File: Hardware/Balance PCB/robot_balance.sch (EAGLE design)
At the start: 49 parts, among them P1 10118194-0001LF, Q1 16Mhz

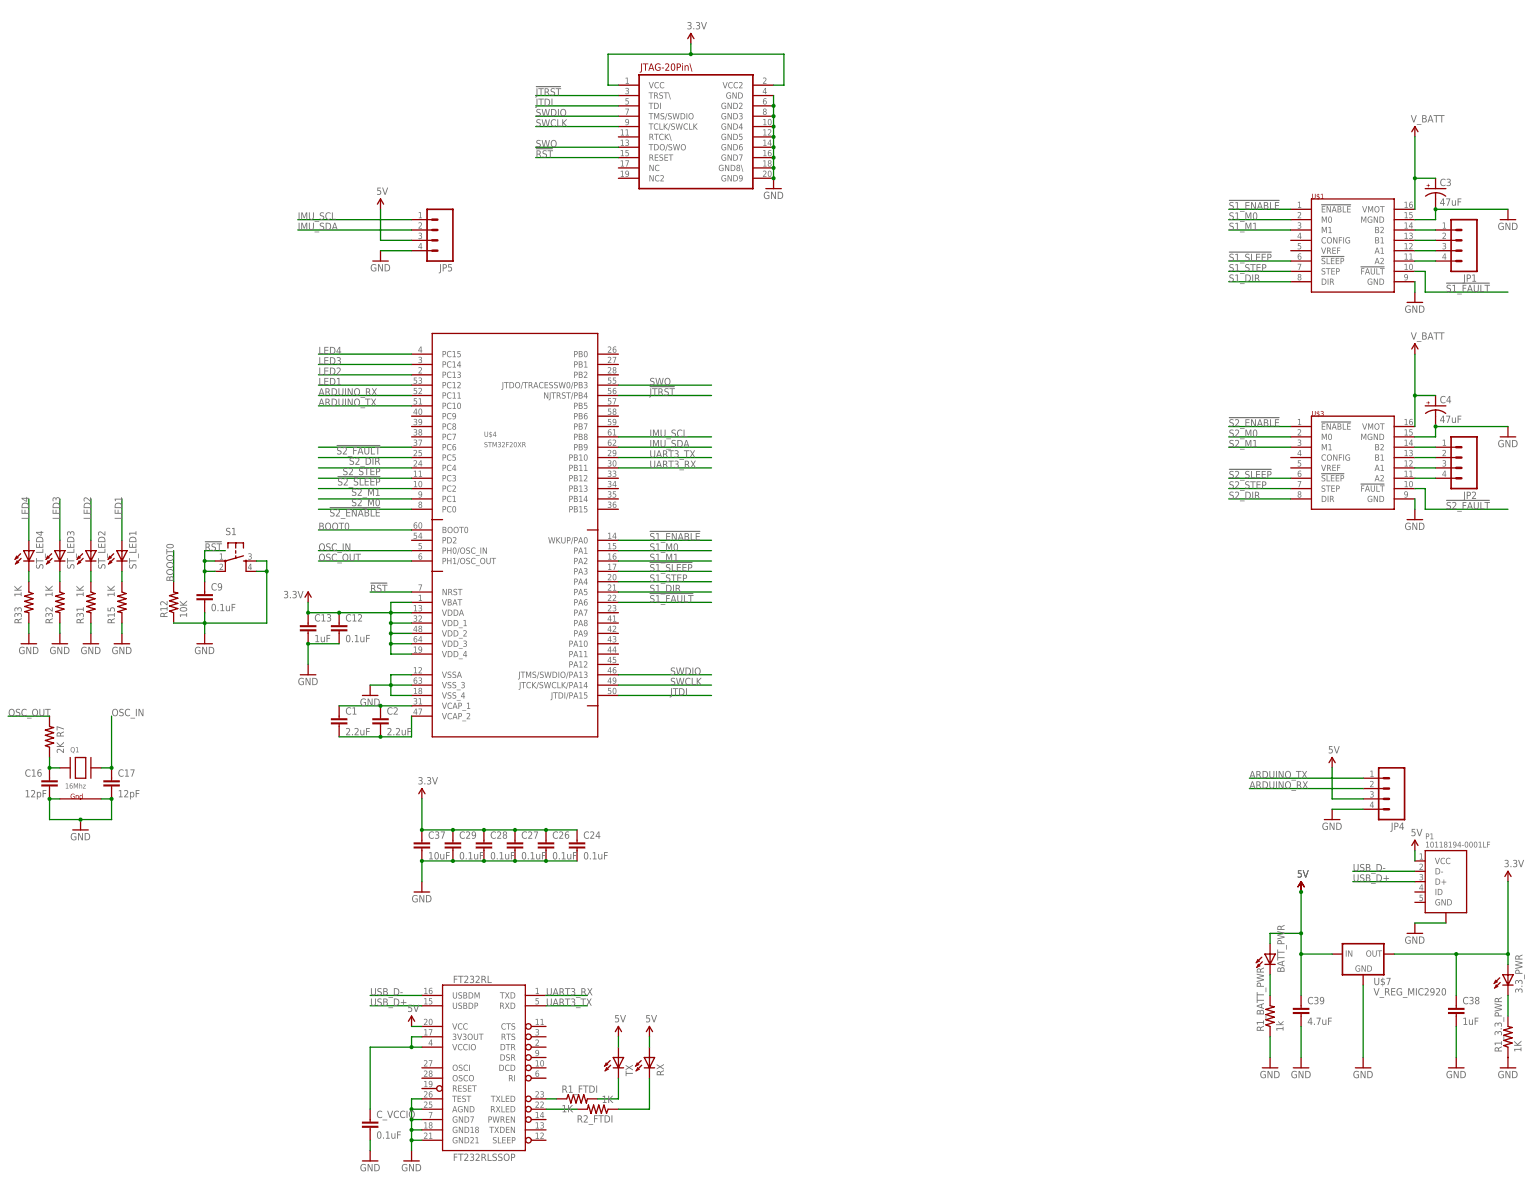
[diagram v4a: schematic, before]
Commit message: changed inter-board connect to 6 pin and added enable line
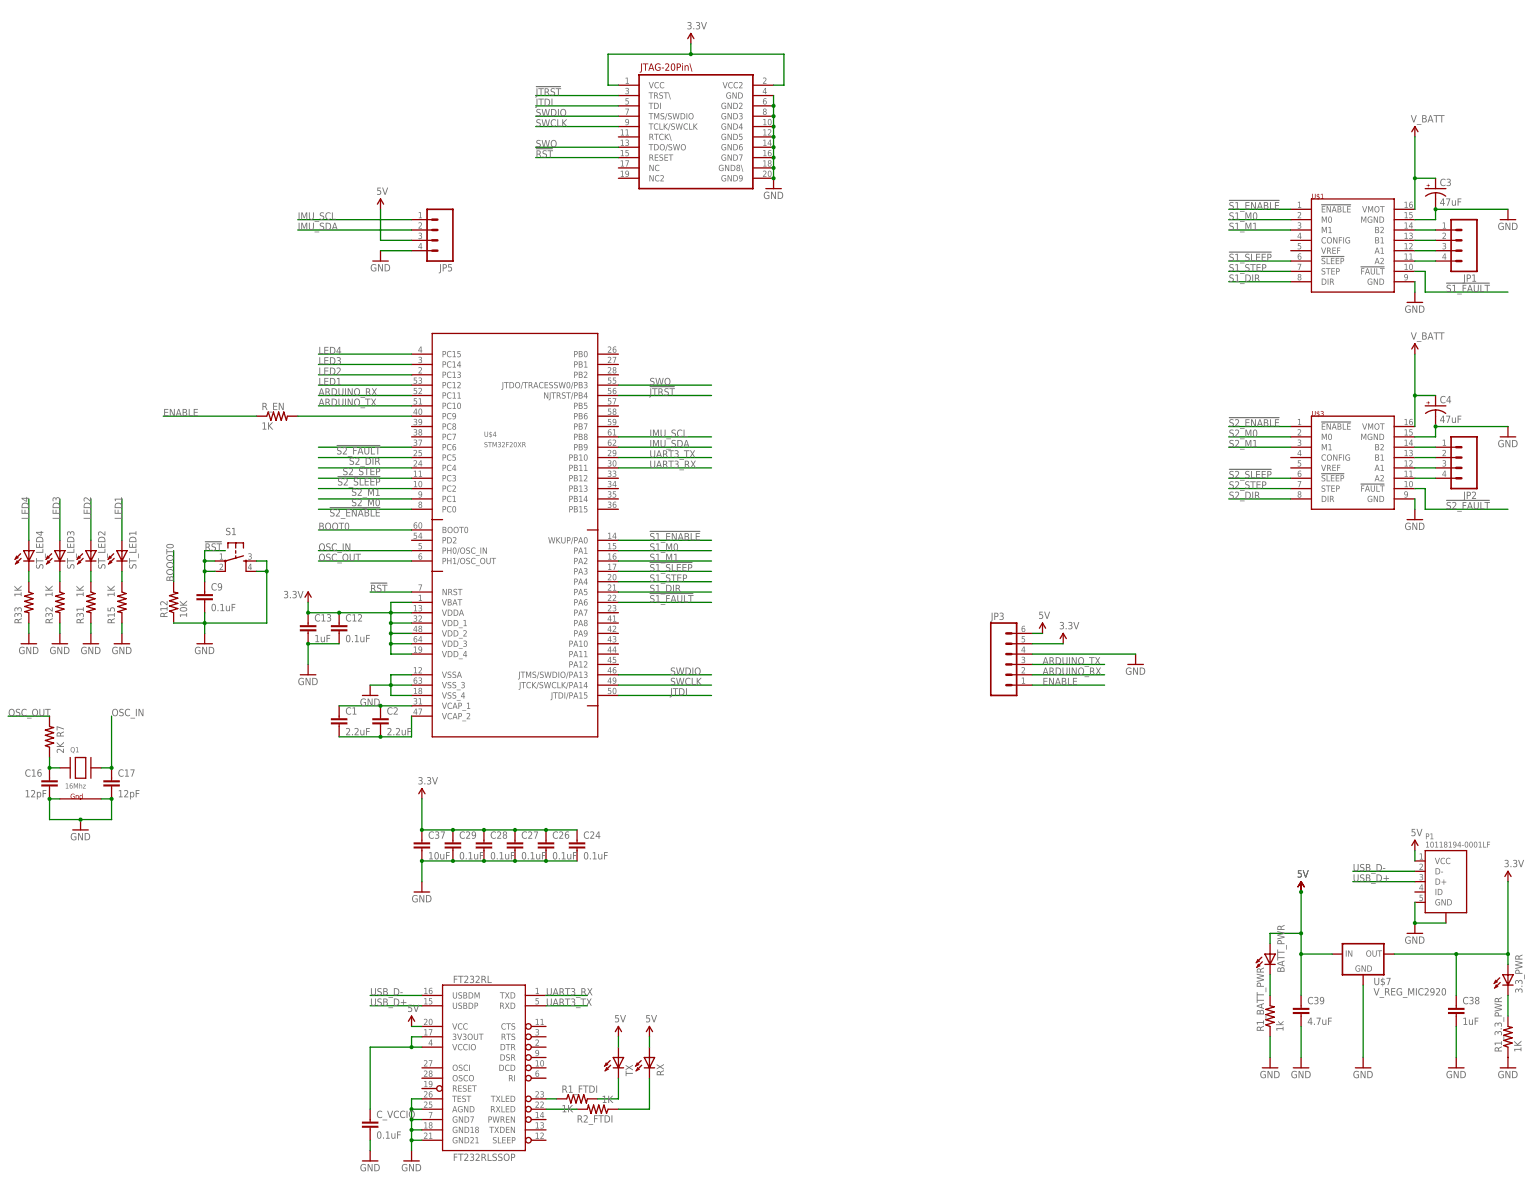
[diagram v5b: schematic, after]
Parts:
- removed JP4: (no value), SparkFun-Connectors:M04POLAR_LOCK
- added JP3: (no value), SparkFun-Connectors:M06POLAR_LOCK
- added R_EN: 1K, SparkFun-Passives:RESISTOR0603-RES
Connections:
- new net ENABLE: JP3.1, R_EN.1
- new net N$6: R_EN.2, U$4.PC9
- net 3.3V: now also JP3.5
- net 5V: now also JP3.6; no longer JP4.3
- net ARDUINO_RX: now also JP3.2; no longer JP4.2
- net ARDUINO_TX: now also JP3.3; no longer JP4.1
- net GND: now also JP3.4, P1.GND; no longer JP4.4
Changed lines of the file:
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@@
 <part name="C4" library="SparkFun-Capacitors" deviceset="47UF-10V-10%(TANT)" device="" value="47uF"/>
 <part name="GND6" library="SparkFun-Aesthetics" deviceset="GND" device=""/>
-<part name="JP4" library="SparkFun-Connectors" deviceset="M04" device="POLAR_LOCK"/>
 <part name="GND7" library="SparkFun-Aesthetics" deviceset="GND" device=""/>
 <part name="JP5" library="SparkFun-Connectors" deviceset="M04" device="POLAR_LOCK"/>
@@
 <part name="P1" library="usb_micro" deviceset="10118194-0001LF" device=""/>
 <part name="SUPPLY13" library="SparkFun-Aesthetics" deviceset="5V" device=""/>
+<part name="JP3" library="SparkFun-Connectors" deviceset="M06" device="POLAR_LOCK"/>
+<part name="SUPPLY14" library="SparkFun-Aesthetics" deviceset="3.3V" device=""/>
+<part name="R_EN" library="SparkFun-Passives" deviceset="RESISTOR" device="0603-RES" value="1K"/>
 </parts>
 <sheets>
@@
 <instance part="C4" gate="G$1" x="317.5" y="-10.16"/>
 <instance part="GND6" gate="1" x="312.42" y="-139.7"/>
-<instance part="JP4" gate="G$1" x="304.8" y="-104.14" rot="R180"/>
-<instance part="GND7" gate="1" x="292.1" y="-111.76"/>
+<instance part="GND7" gate="1" x="243.84" y="-73.66"/>
 <instance part="JP5" gate="G$1" x="71.12" y="33.02" rot="R180"/>
 <instance part="GND9" gate="1" x="58.42" y="25.4"/>
@@
 <instance part="SUPPLY5" gate="G$1" x="284.48" y="-129.54"/>
 <instance part="SUPPLY7" gate="G$1" x="284.48" y="-129.54"/>
-<instance part="SUPPLY8" gate="G$1" x="292.1" y="-99.06"/>
+<instance part="SUPPLY8" gate="G$1" x="220.98" y="-66.04"/>
 <instance part="SUPPLY6" gate="G$1" x="58.42" y="38.1"/>
 <instance part="GND10" gate="1" x="66.04" y="-195.58"/>
@@
 <instance part="P1" gate="G$1" x="317.5" y="-127"/>
 <instance part="SUPPLY13" gate="G$1" x="312.42" y="-119.38"/>
+<instance part="JP3" gate="G$1" x="213.36" y="-73.66"/>
+<instance part="SUPPLY14" gate="G$1" x="226.06" y="-68.58"/>
+<instance part="R_EN" gate="G$1" x="33.02" y="-12.7"/>
 </instances>
 <busses>
@@
 <wire x1="312.42" y1="-137.16" x2="320.04" y2="-137.16" width="0.1524" layer="91"/>
 <pinref part="P1" gate="G$1" pin="SHIELD"/>
+<pinref part="P1" gate="G$1" pin="GND"/>
+<wire x1="312.42" y1="-132.08" x2="312.42" y2="-137.16" width="0.1524" layer="91"/>
+<junction x="312.42" y="-137.16"/>
 </segment>
 <segment>
 <pinref part="GND7" gate="1" pin="GND"/>
-<pinref part="JP4" gate="G$1" pin="4"/>
-<wire x1="292.1" y1="-109.22" x2="299.72" y2="-109.22" width="0.1524" layer="91"/>
+<wire x1="243.84" y1="-71.12" x2="218.44" y2="-71.12" width="0.1524" layer="91"/>
+<pinref part="JP3" gate="G$1" pin="4"/>
 </segment>
 <segment>
@@
 <junction x="134.62" y="76.2"/>
 </segment>
+<segment>
+<pinref part="JP3" gate="G$1" pin="5"/>
+<pinref part="SUPPLY14" gate="G$1" pin="3.3V"/>
+<wire x1="226.06" y1="-68.58" x2="218.44" y2="-68.58" width="0.1524" layer="91"/>
+</segment>
 </net>
 <net name="V_USB" class="3">
@@
 <net name="ARDUINO_TX" class="1">
 <segment>
-<pinref part="JP4" gate="G$1" pin="1"/>
-<wire x1="299.72" y1="-101.6" x2="271.78" y2="-101.6" width="0.1524" layer="91"/>
-<label x="271.78" y="-101.6" size="1.778" layer="95"/>
+<wire x1="218.44" y1="-73.66" x2="236.22" y2="-73.66" width="0.1524" layer="91"/>
+<label x="220.98" y="-73.66" size="1.778" layer="95"/>
+<pinref part="JP3" gate="G$1" pin="3"/>
 </segment>
 <segment>
@@
 <net name="ARDUINO_RX" class="1">
 <segment>
-<pinref part="JP4" gate="G$1" pin="2"/>
-<wire x1="299.72" y1="-104.14" x2="271.78" y2="-104.14" width="0.1524" layer="91"/>
-<label x="271.78" y="-104.14" size="1.778" layer="95"/>
+<wire x1="218.44" y1="-76.2" x2="236.22" y2="-76.2" width="0.1524" layer="91"/>
+<label x="220.98" y="-76.2" size="1.778" layer="95"/>
+<pinref part="JP3" gate="G$1" pin="2"/>
 </segment>
 <segment>
@@
 </segment>
 <segment>
-<pinref part="JP4" gate="G$1" pin="3"/>
-<wire x1="299.72" y1="-106.68" x2="292.1" y2="-106.68" width="0.1524" layer="91"/>
-<wire x1="292.1" y1="-106.68" x2="292.1" y2="-99.06" width="0.1524" layer="91"/>
+<wire x1="218.44" y1="-66.04" x2="220.98" y2="-66.04" width="0.1524" layer="91"/>
 <pinref part="SUPPLY8" gate="G$1" pin="5V"/>
+<pinref part="JP3" gate="G$1" pin="6"/>
 </segment>
 <segment>
@@
 </segment>
 </net>
+<net name="ENABLE" class="0">
+<segment>
+<pinref part="JP3" gate="G$1" pin="1"/>
+<wire x1="218.44" y1="-78.74" x2="236.22" y2="-78.74" width="0.1524" layer="91"/>
+<label x="220.98" y="-78.74" size="1.778" layer="95"/>
+</segment>
+<segment>
+<pinref part="R_EN" gate="G$1" pin="1"/>
+<wire x1="27.94" y1="-12.7" x2="5.08" y2="-12.7" width="0.1524" layer="91"/>
+<label x="5.08" y="-12.7" size="1.778" layer="95"/>
+</segment>
+</net>
+<net name="N$6" class="0">
+<segment>
+<pinref part="U$4" gate="G$1" pin="PC9"/>
+<pinref part="R_EN" gate="G$1" pin="2"/>
+<wire x1="38.1" y1="-12.7" x2="66.04" y2="-12.7" width="0.1524" layer="91"/>
+</segment>
+</net>

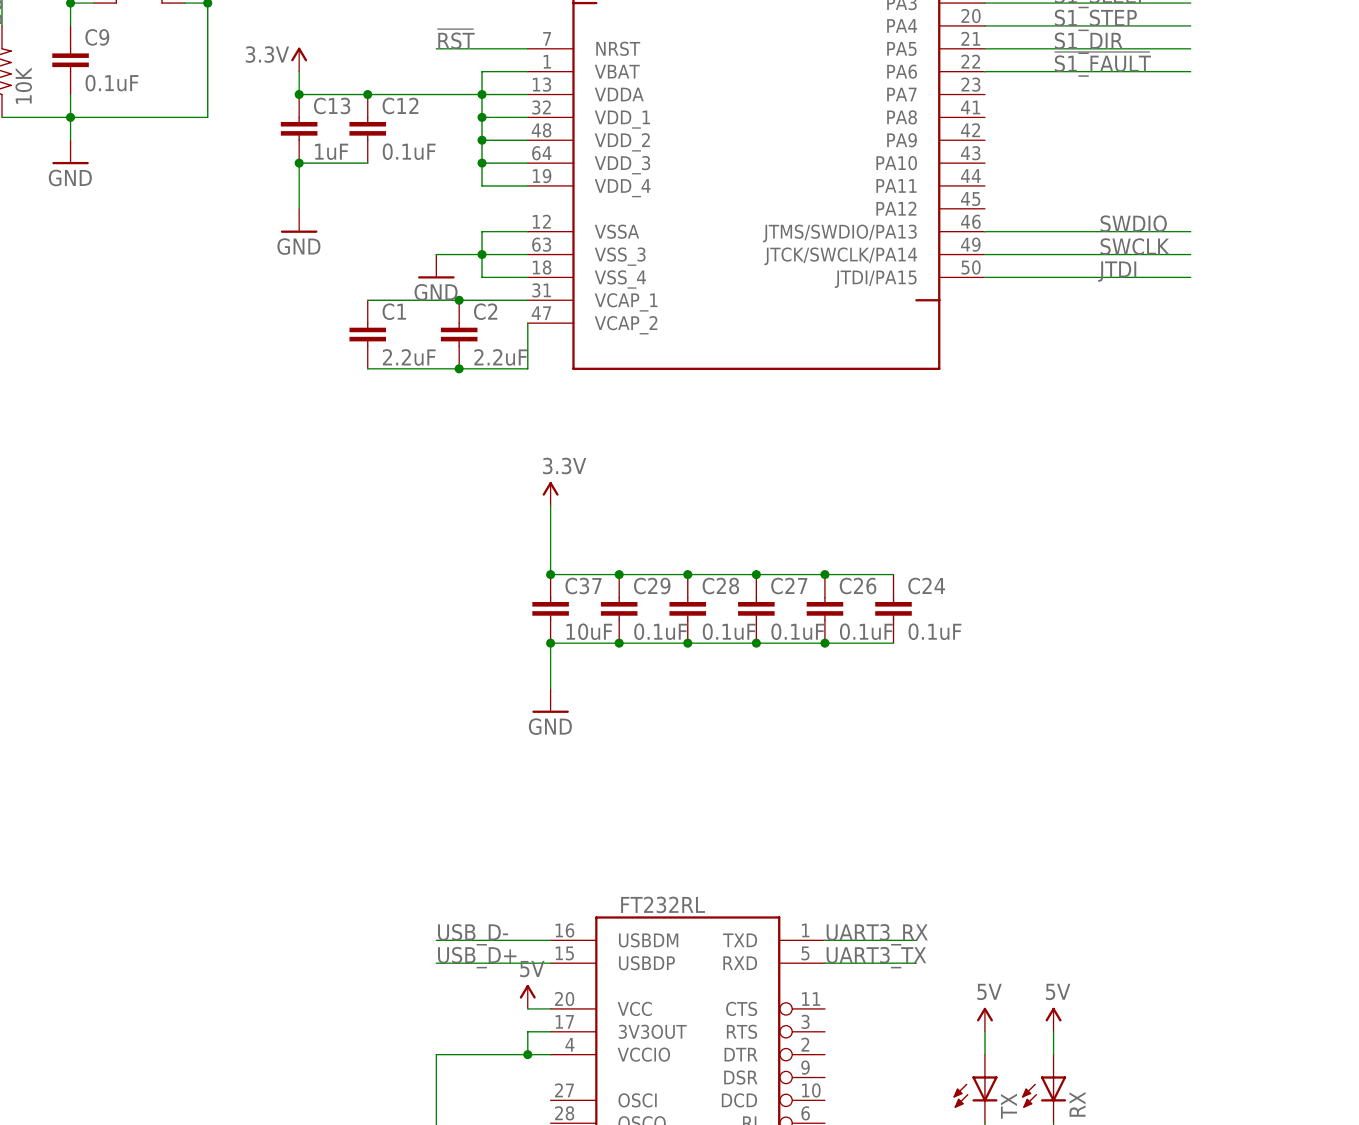
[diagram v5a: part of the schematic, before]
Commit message: Added VCP solder jumpers
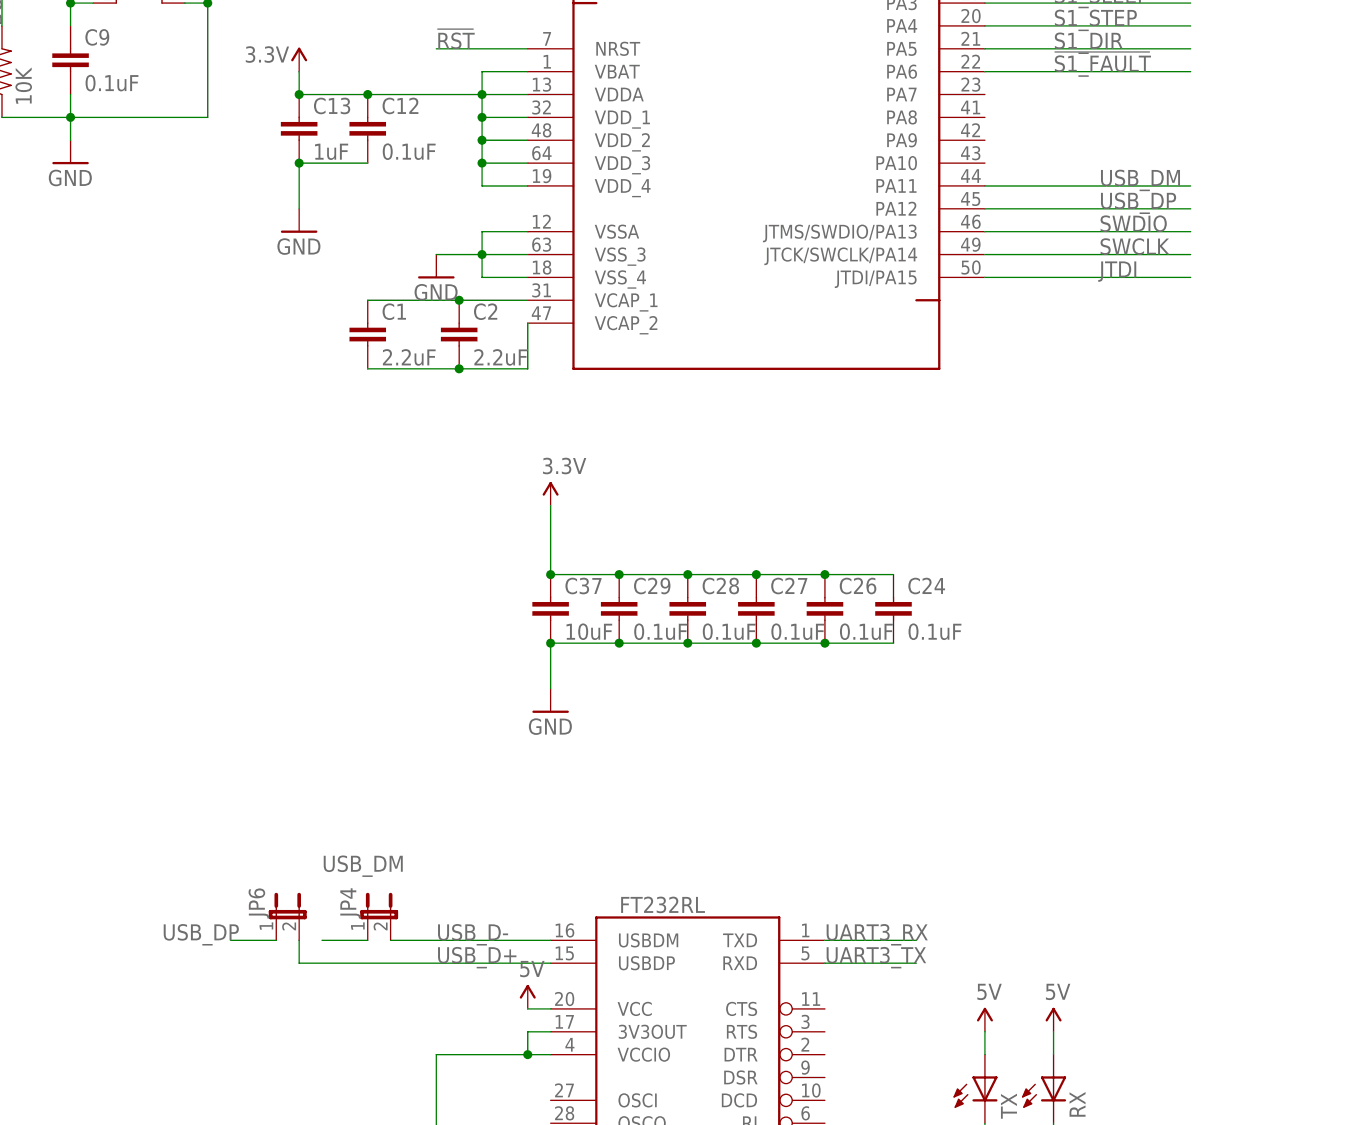
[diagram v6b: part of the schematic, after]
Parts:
- added JP4, JP6: (no value), SparkFun-Retired:JUMPER-2SMD-NO
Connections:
- new net USB_DM: JP4.1, U$4.PA11
- new net USB_DP: JP6.1, U$4.PA12
- net USB_D+: now also JP6.2
- net USB_D-: now also JP4.2
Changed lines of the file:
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@@
 <part name="SUPPLY14" library="SparkFun-Aesthetics" deviceset="3.3V" device=""/>
 <part name="R_EN" library="SparkFun-Passives" deviceset="RESISTOR" device="0603-RES" value="1K"/>
+<part name="JP4" library="SparkFun-Retired" deviceset="JUMPER-2" device="SMD-NO"/>
+<part name="JP6" library="SparkFun-Retired" deviceset="JUMPER-2" device="SMD-NO"/>
 </parts>
 <sheets>
@@
 <instance part="SUPPLY14" gate="G$1" x="226.06" y="-68.58"/>
 <instance part="R_EN" gate="G$1" x="33.02" y="-12.7"/>
+<instance part="JP4" gate="A" x="48.26" y="-152.4"/>
+<instance part="JP6" gate="A" x="38.1" y="-152.4"/>
 </instances>
 <busses>
@@
 <segment>
 <pinref part="FT232RL" gate="G$1" pin="USBDM"/>
-<wire x1="55.88" y1="-154.94" x2="68.58" y2="-154.94" width="0.1524" layer="91"/>
+<wire x1="50.8" y1="-154.94" x2="68.58" y2="-154.94" width="0.1524" layer="91"/>
 <label x="55.88" y="-154.94" size="1.778" layer="95"/>
+<pinref part="JP4" gate="A" pin="2"/>
 </segment>
 <segment>
@@
 <net name="USB_D+" class="1">
 <segment>
-<wire x1="55.88" y1="-157.48" x2="68.58" y2="-157.48" width="0.1524" layer="91"/>
 <pinref part="FT232RL" gate="G$1" pin="USBDP"/>
 <label x="55.88" y="-157.48" size="1.778" layer="95"/>
+<pinref part="JP6" gate="A" pin="2"/>
+<wire x1="68.58" y1="-157.48" x2="40.64" y2="-157.48" width="0.1524" layer="91"/>
+<wire x1="40.64" y1="-157.48" x2="40.64" y2="-154.94" width="0.1524" layer="91"/>
 </segment>
 <segment>
@@
 </segment>
 </net>
+<net name="USB_DM" class="0">
+<segment>
+<pinref part="JP4" gate="A" pin="1"/>
+<wire x1="48.26" y1="-154.94" x2="43.18" y2="-154.94" width="0.1524" layer="91"/>
+<label x="43.18" y="-147.32" size="1.778" layer="95"/>
+</segment>
+<segment>
+<pinref part="U$4" gate="G$1" pin="PA11"/>
+<wire x1="116.84" y1="-71.12" x2="139.7" y2="-71.12" width="0.1524" layer="91"/>
+<label x="129.54" y="-71.12" size="1.778" layer="95"/>
+</segment>
+</net>
+<net name="USB_DP" class="0">
+<segment>
+<pinref part="JP6" gate="A" pin="1"/>
+<wire x1="38.1" y1="-154.94" x2="33.02" y2="-154.94" width="0.1524" layer="91"/>
+<label x="25.4" y="-154.94" size="1.778" layer="95"/>
+</segment>
+<segment>
+<pinref part="U$4" gate="G$1" pin="PA12"/>
+<wire x1="116.84" y1="-73.66" x2="139.7" y2="-73.66" width="0.1524" layer="91"/>
+<label x="129.54" y="-73.66" size="1.778" layer="95"/>
+</segment>
+</net>
